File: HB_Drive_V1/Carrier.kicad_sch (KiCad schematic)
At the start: 30 parts, among them J1002 Conn_02x04_Odd_Even, U1001 NE555D, U1003 TL082, U1004 TL082

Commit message: Updates to 1st review corrected V2 of board
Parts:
- C1002: value 100pF 50V -> 200pF 50V
- C1003: value 100pF 50V -> 400pF 50V
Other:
- moved on the sheet: C1001, C1002, C1003, C1004, C1005, C1006, C1007, C1008, C1009, C1011, C1013, C1014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

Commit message: restores v2 to condtion as ordered!
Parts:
- C1003: value 400pF 50V -> 470pF 50V
- R1010: value 1MΩ 5% -> 5MΩ 5%
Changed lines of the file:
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@@
 			)
 		)
-		(property "Value" "1MΩ 5%"
+		(property "Value" "5MΩ 5%"
 			(at 156.972 48.514 90)
 			(show_name no)
@@
 			)
 		)
-		(property "Value" "400pF 50V"
+		(property "Value" "470pF 50V"
 			(at 223.774 41.402 90)
 			(show_name no)

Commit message: Brings everything up to latest copy on my computer
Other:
- company: (none) -> UW Madison, WEMPEC
- title: (none) -> HB Drive V3
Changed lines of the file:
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@@
 	(generator_version "10.0")
 	(paper "A4")
+	(title_block
+		(title "HB Drive V3")
+		(date "2026-09-08")
+		(company "UW Madison, WEMPEC")
+	)
 	(rectangle
 		(start 138.938 130.556)

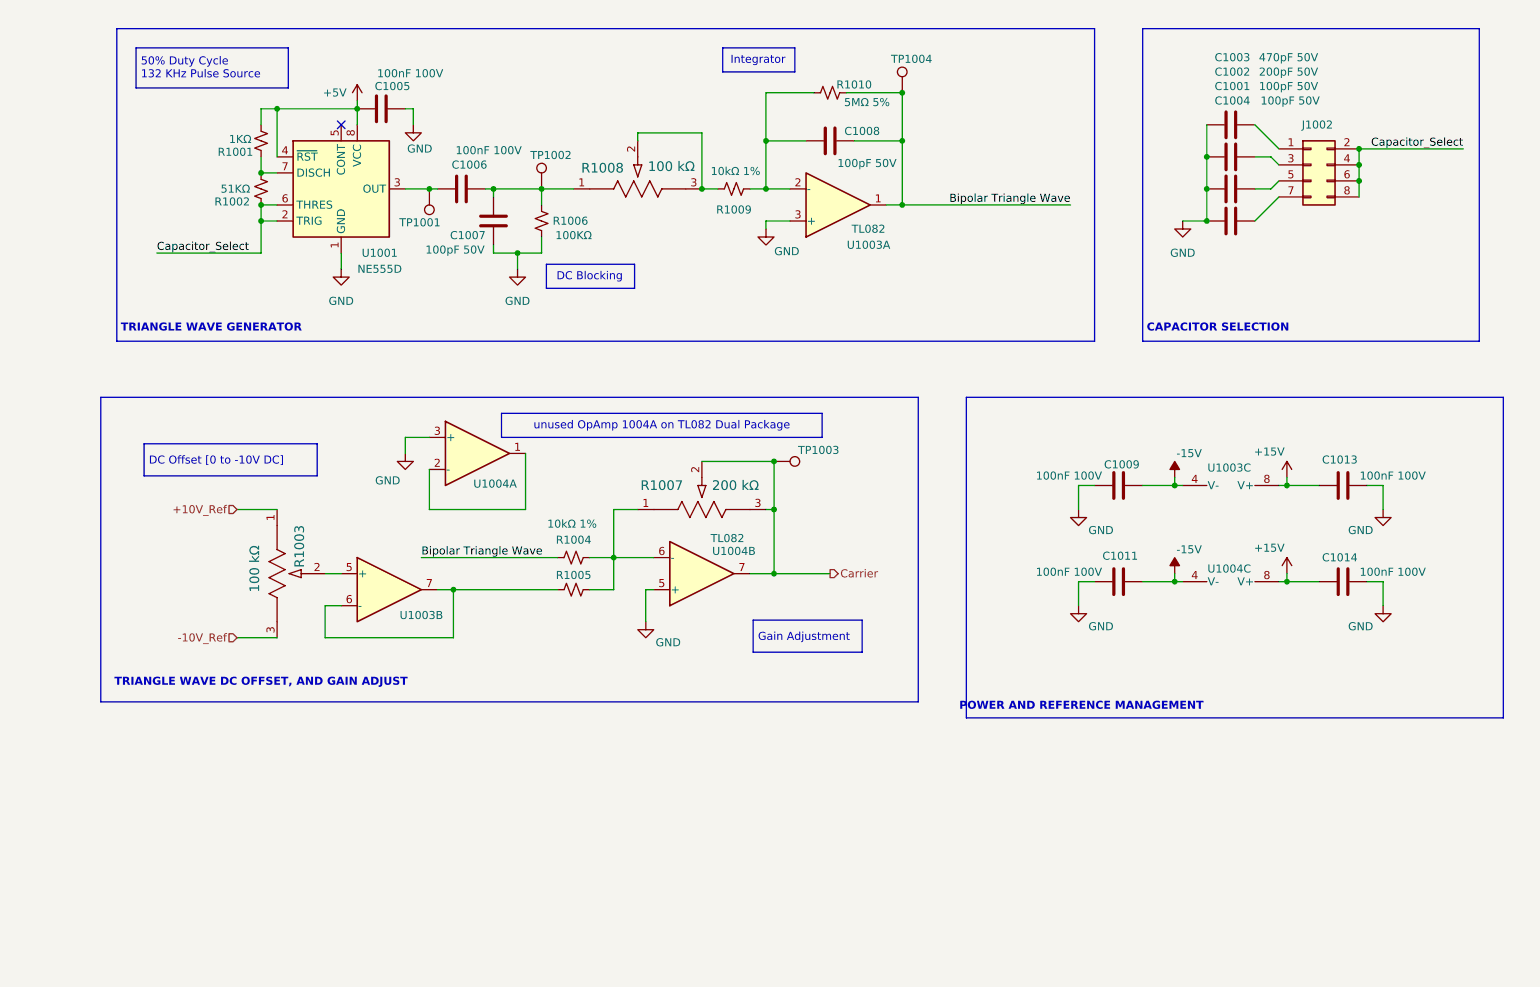
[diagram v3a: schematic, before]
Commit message: Makes annotation changes
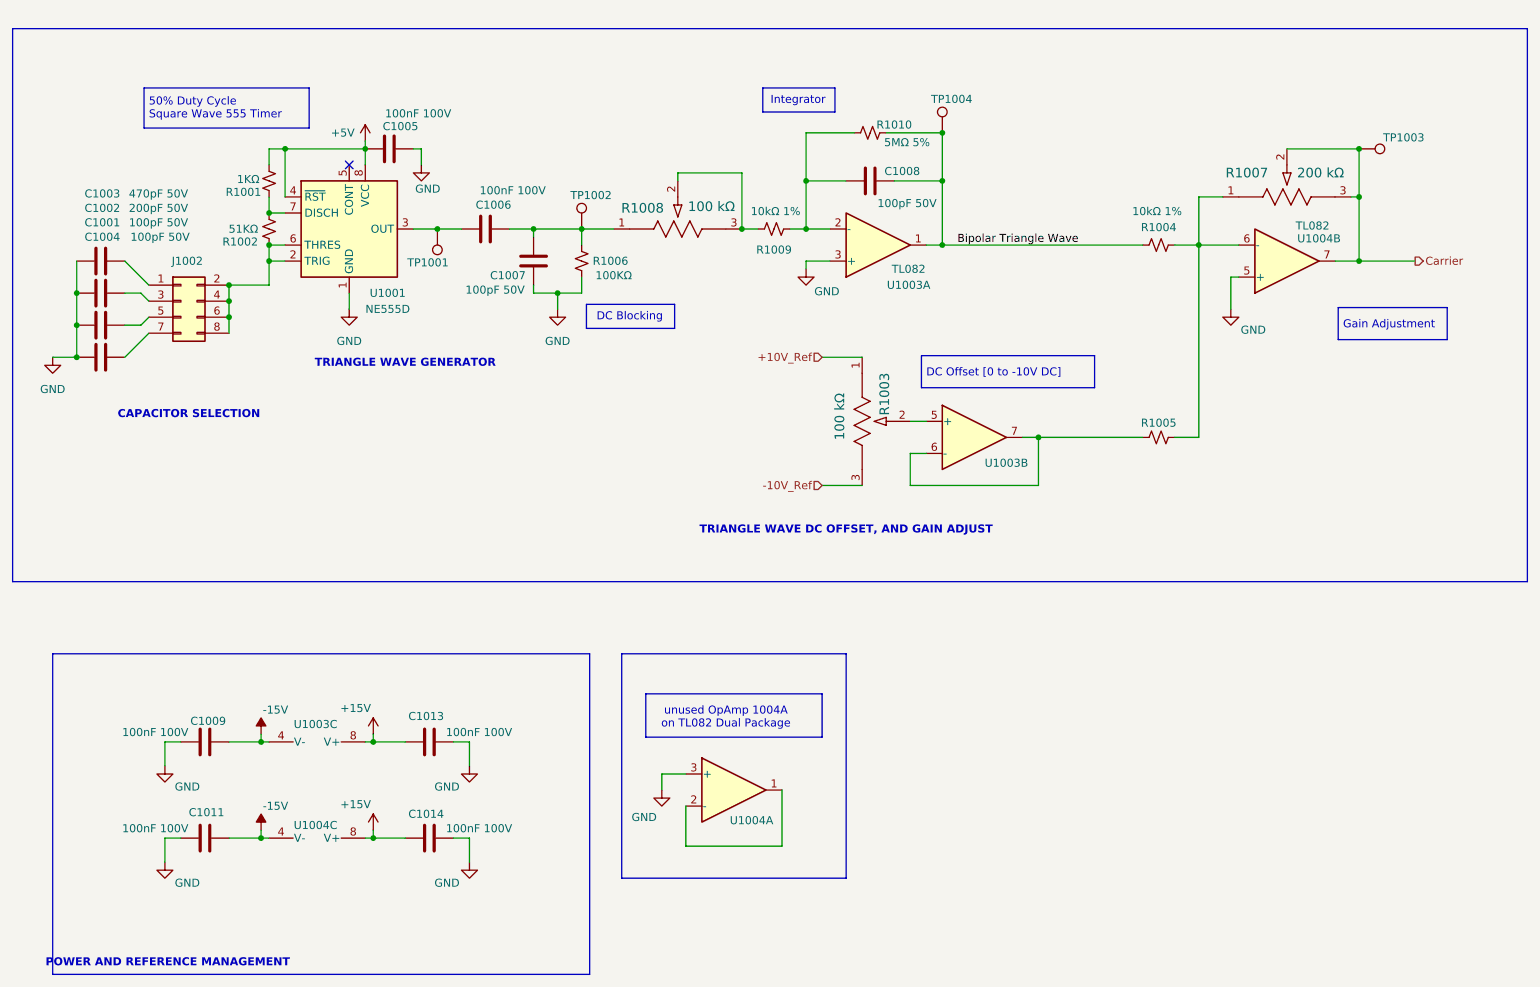
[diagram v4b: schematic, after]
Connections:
- net Capacitor_Select: no longer names the net of J1002.2 (Pin_2), J1002.4 (Pin_4), J1002.6 (Pin_6), J1002.8 (Pin_8), R1002.2, U1001.2 (TRIG), U1001.6 (THRES)
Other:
- note added: "50% Duty Cycle Square Wave 555 Timer"
- note removed: "50% Duty Cycle 132 KHz Pulse Source"
- moved on the sheet: C1001, C1002, C1003, C1004, C1005, C1006, C1007, C1008, C1009, C1011, C1013, C1014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
